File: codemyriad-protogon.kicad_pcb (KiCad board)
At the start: 2 copper layers, 54.3 x 36.6 mm, 14 parts, among them J1 Hexpansion-Connector, J2 Conn_02x10_Odd_Even, P1 PZ254V-11-02P, U1 ZD24C64A-XGMT, U2 SM04B-SRSS-TB_(LF)(SN)

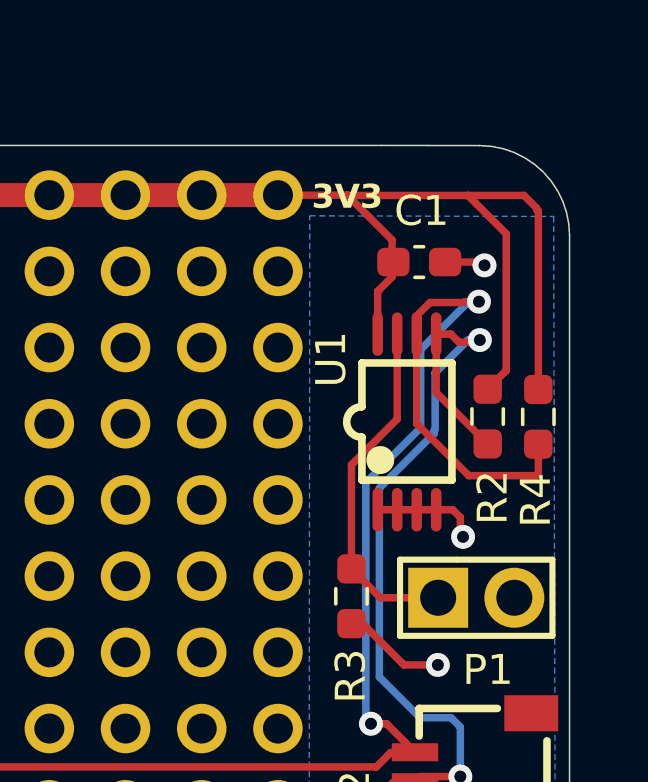
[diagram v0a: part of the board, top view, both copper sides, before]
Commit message: Rework the P1 jumper so it write-protects the EEPROM
P1 pin 2 now goes to +3V3 instead of GND, so shorting the jumper pulls WP
high and write-protects the EEPROM after provisioning. R3 still pulls WP low,
so the part is writable by default for the badge to provision. Board files
from the designer's reworked version.

- Update .kicad_pcb / .kicad_sch (reworked P1 net + routing)
- Regenerate fabrication outputs (gerbers, drill, STEP, DRC: 0 errors, 0 unconnected)
- Re-render top/bottom/perspective with P1 shown, now that it's functional
- README: document short-P1-to-write-protect

Co-Authored-By: Claude Opus 4.8 (1M context) <noreply@anthropic.com>
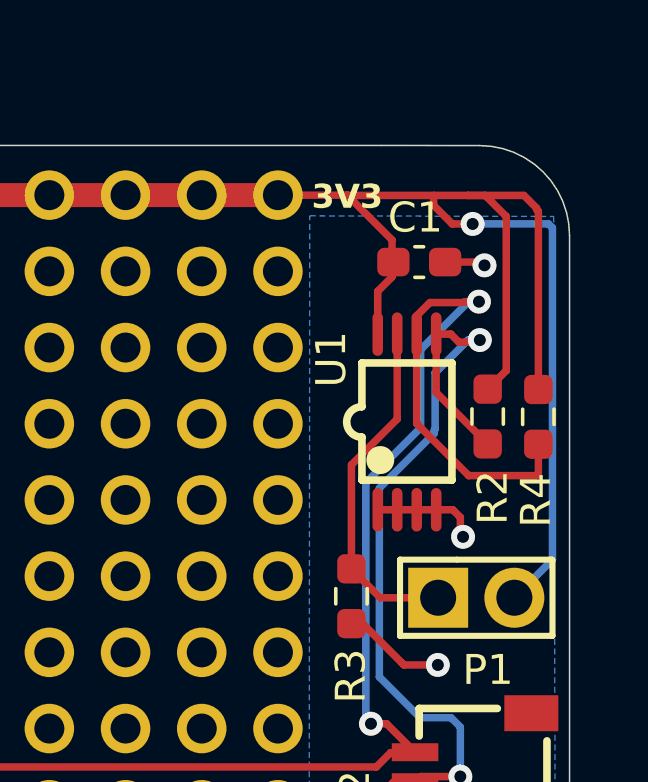
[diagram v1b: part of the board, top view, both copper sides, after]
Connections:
- P1 pad 2: GND -> +3.3V
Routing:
- net +3.3V: track 136.9 -> 154.7 mm, vias 0 -> 1
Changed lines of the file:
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@@
 		(tags "capacitor handsolder")
 		(property "Reference" "C1"
-			(at 0.08 -1.7 0)
+			(at -0.13 -1.48 0)
 			(layer "F.SilkS")
 			(effects
@@
 			(layers "*.Cu" "*.Mask")
 			(remove_unused_layers no)
-			(net 13 "GND")
+			(net 15 "+3.3V")
 			(pinfunction "2")
 			(pintype "unspecified")
@@
 	)
 	(segment
+		(start 151.46 83.48)
+		(end 150.88 83.48)
+		(width 0.25)
+		(layer "F.Cu")
+		(net 15)
+	)
+	(segment
 		(start 119.89 100.6)
 		(end 120.54 101.25)
@@
 	)
 	(segment
+		(start 151.54 89.9375)
+		(end 152.16 89.3175)
+		(width 0.25)
+		(layer "F.Cu")
+		(net 15)
+	)
+	(segment
 		(start 133.12 100)
 		(end 133.12 83.47)
@@
 	)
 	(segment
+		(start 152.16 84.18)
+		(end 151.46 83.48)
+		(width 0.25)
+		(layer "F.Cu")
+		(net 15)
+	)
+	(segment
 		(start 121.38 83.47)
 		(end 121.13 83.22)
@@
 	)
 	(segment
+		(start 149.74 83.81)
+		(end 149.74 83.48)
+		(width 0.25)
+		(layer "F.Cu")
+		(net 15)
+	)
+	(segment
 		(start 148.353213 84.963213)
 		(end 148.353213 86.196787)
@@
 	)
 	(segment
-		(start 152.16 84.76)
-		(end 150.88 83.48)
-		(width 0.25)
-		(layer "F.Cu")
-		(net 15)
-	)
-	(segment
 		(start 153.23 84)
 		(end 153.23 89.9475)
@@
 	(segment
 		(start 150.88 83.48)
-		(end 146.87 83.48)
+		(end 149.74 83.48)
 		(width 0.25)
 		(layer "F.Cu")
@@
 	)
 	(segment
-		(start 151.54 89.9375)
-		(end 152.16 89.3175)
-		(width 0.25)
-		(layer "F.Cu")
-		(net 15)
-	)
-	(segment
-		(start 152.16 89.3175)
-		(end 152.16 84.76)
+		(start 149.74 83.48)
+		(end 146.87 83.48)
 		(width 0.25)
 		(layer "F.Cu")
@@
 	)
 	(segment
+		(start 150.36 84.43)
+		(end 149.74 83.81)
+		(width 0.25)
+		(layer "F.Cu")
+		(net 15)
+	)
+	(segment
+		(start 151.04 84.43)
+		(end 150.36 84.43)
+		(width 0.25)
+		(layer "F.Cu")
+		(net 15)
+	)
+	(segment
+		(start 152.16 89.3175)
+		(end 152.16 84.18)
+		(width 0.25)
+		(layer "F.Cu")
+		(net 15)
+	)
+	(segment
 		(start 100.9 100.6)
 		(end 119.89 100.6)
@@
 		(net 15)
 	)
+	(via
+		(at 151.04 84.43)
+		(size 0.8)
+		(drill 0.4)
+		(layers "F.Cu" "B.Cu")
+		(net 15)
+	)
+	(segment
+		(start 151.04 84.43)
+		(end 153.57 84.43)
+		(width 0.25)
+		(layer "B.Cu")
+		(net 15)
+	)
+	(segment
+		(start 153.57 84.43)
+		(end 153.7 84.56)
+		(width 0.25)
+		(layer "B.Cu")
+		(net 15)
+	)
+	(segment
+		(start 153.7 95.620003)
+		(end 152.430003 96.89)
+		(width 0.25)
+		(layer "B.Cu")
+		(net 15)
+	)
+	(segment
+		(start 153.7 84.56)
+		(end 153.7 95.620003)
+		(width 0.25)
+		(layer "B.Cu")
+		(net 15)
+	)

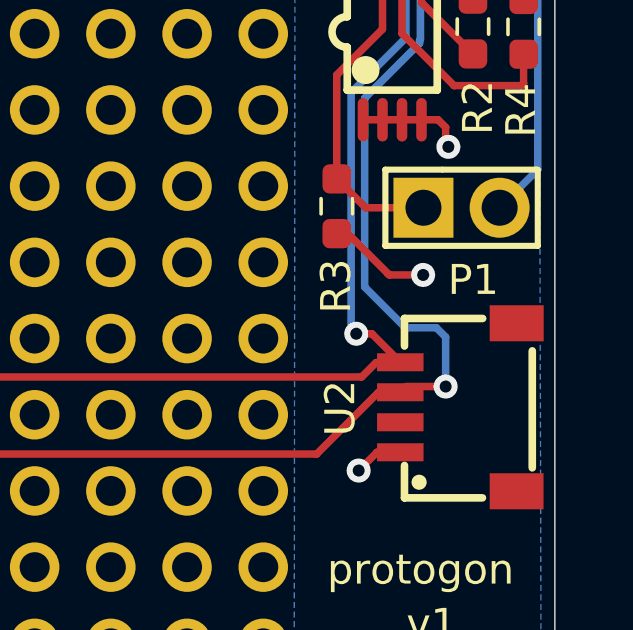
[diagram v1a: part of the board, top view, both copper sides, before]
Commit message: Route the Qwiic VCC; board is DRC/ERC clean and order-ready
The designer routed the one remaining track (U2 pin 2 → +3.3V), closing the
Qwiic-power bug from the review. Board files are from their KiCad save;
fabrication outputs and renders regenerated to match.

- U2.2 Qwiic VCC now on +3.3V and routed: DRC 0 errors, 0 unconnected
- ERC clean; no orphan nets
- Re-verified vs spec: edge-connector pinout (all 20), EEPROM at 0x50,
  SDA/SCL, 4K7 pull-ups, WP jumper, decoupling, detect→GND
- Regenerate gerbers, drill, STEP, positions, DRC report, renders

Co-Authored-By: Claude Opus 4.8 (1M context) <noreply@anthropic.com>
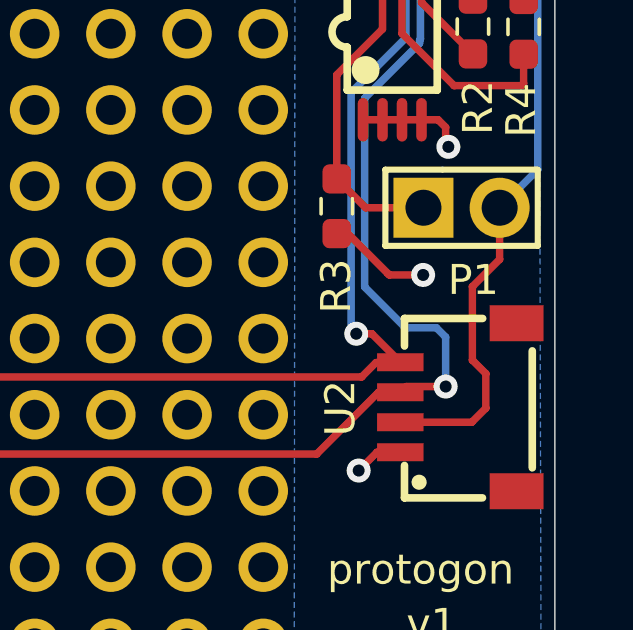
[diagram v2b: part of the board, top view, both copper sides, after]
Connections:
- U2 pad 2: /3V3 -> +3.3V
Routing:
- net +3.3V: track 154.7 -> 165.0 mm
